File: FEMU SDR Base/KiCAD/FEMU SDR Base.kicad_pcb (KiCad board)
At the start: 4 copper layers, 164.8 x 164.8 mm, 94 parts, among them M1 M1, M10 M1, M11 M1, M12 M1, M13 M1, M14 M1, M15 M1, M16 M1, M2 M1, M3 M1, M4 M1, M5 M1, M6 M1, M7 M1, M8 M1, M9 M1, P1 Battery, P10 PWM2, P11 PWM3, P12 PWM4, P13 PWM1, P14 PWM2, P15 PWM3, P16 PWM4, P17 12V, P18 GND, P19 12V, P2 SDR_Shield_1, P20 GND, P21 SDR0, P22 SDR1, P27 PWM0, P28 PWM5, P29 PWM6, P3 SDR_Shield_2, P30 PWM7, P31 PWM0, P32 PWM5, P33 PWM6, P34 PWM7, P35 Battery, P36 RPi, P37 PXH, P38 Rx, P4 12V, P5 GND, P6 12V, P7 GND, P8 Raspi_Power_Shield, P9 PWM1, U1 TPS562209, U2 LP38858-LDO, U3 LP38858-LDO, U4 7833, U5 7833

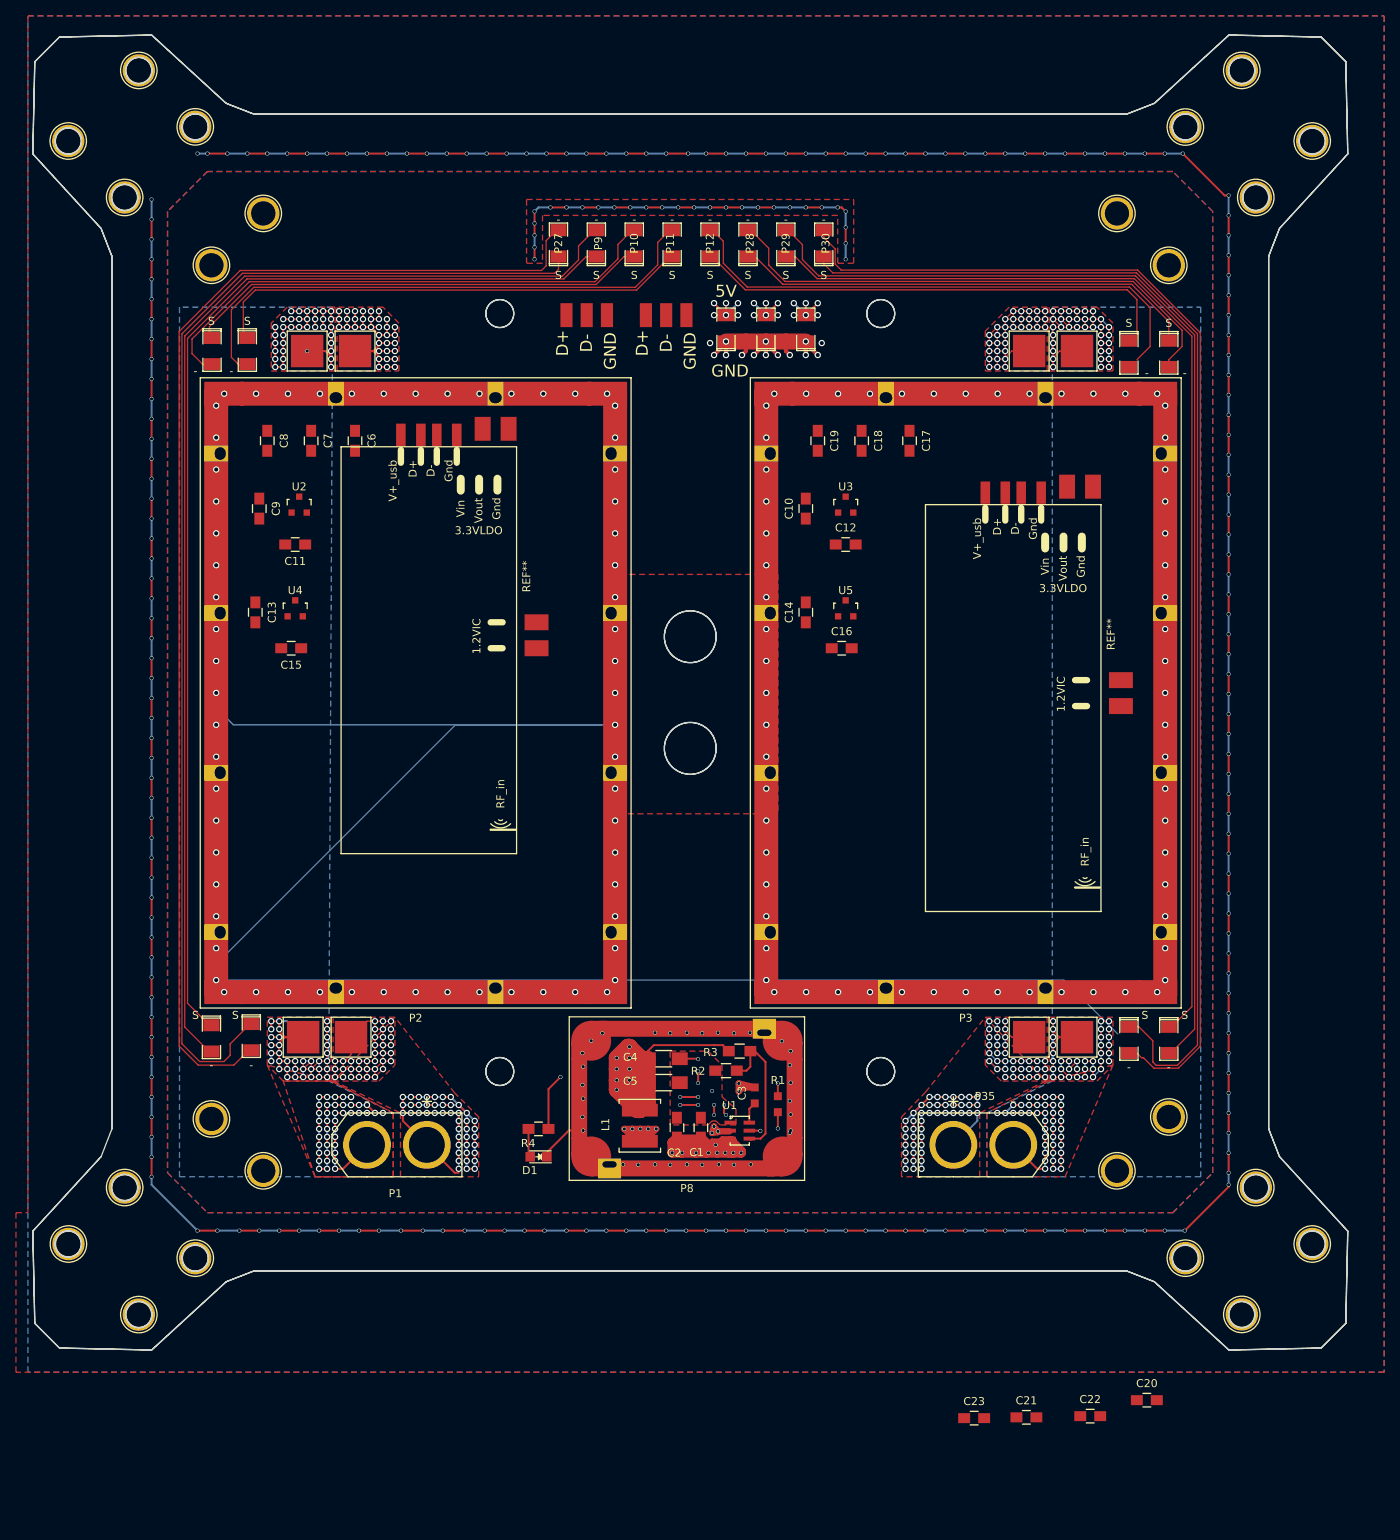
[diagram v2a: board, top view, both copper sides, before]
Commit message: STATUS=FREE, SDR1 arranged
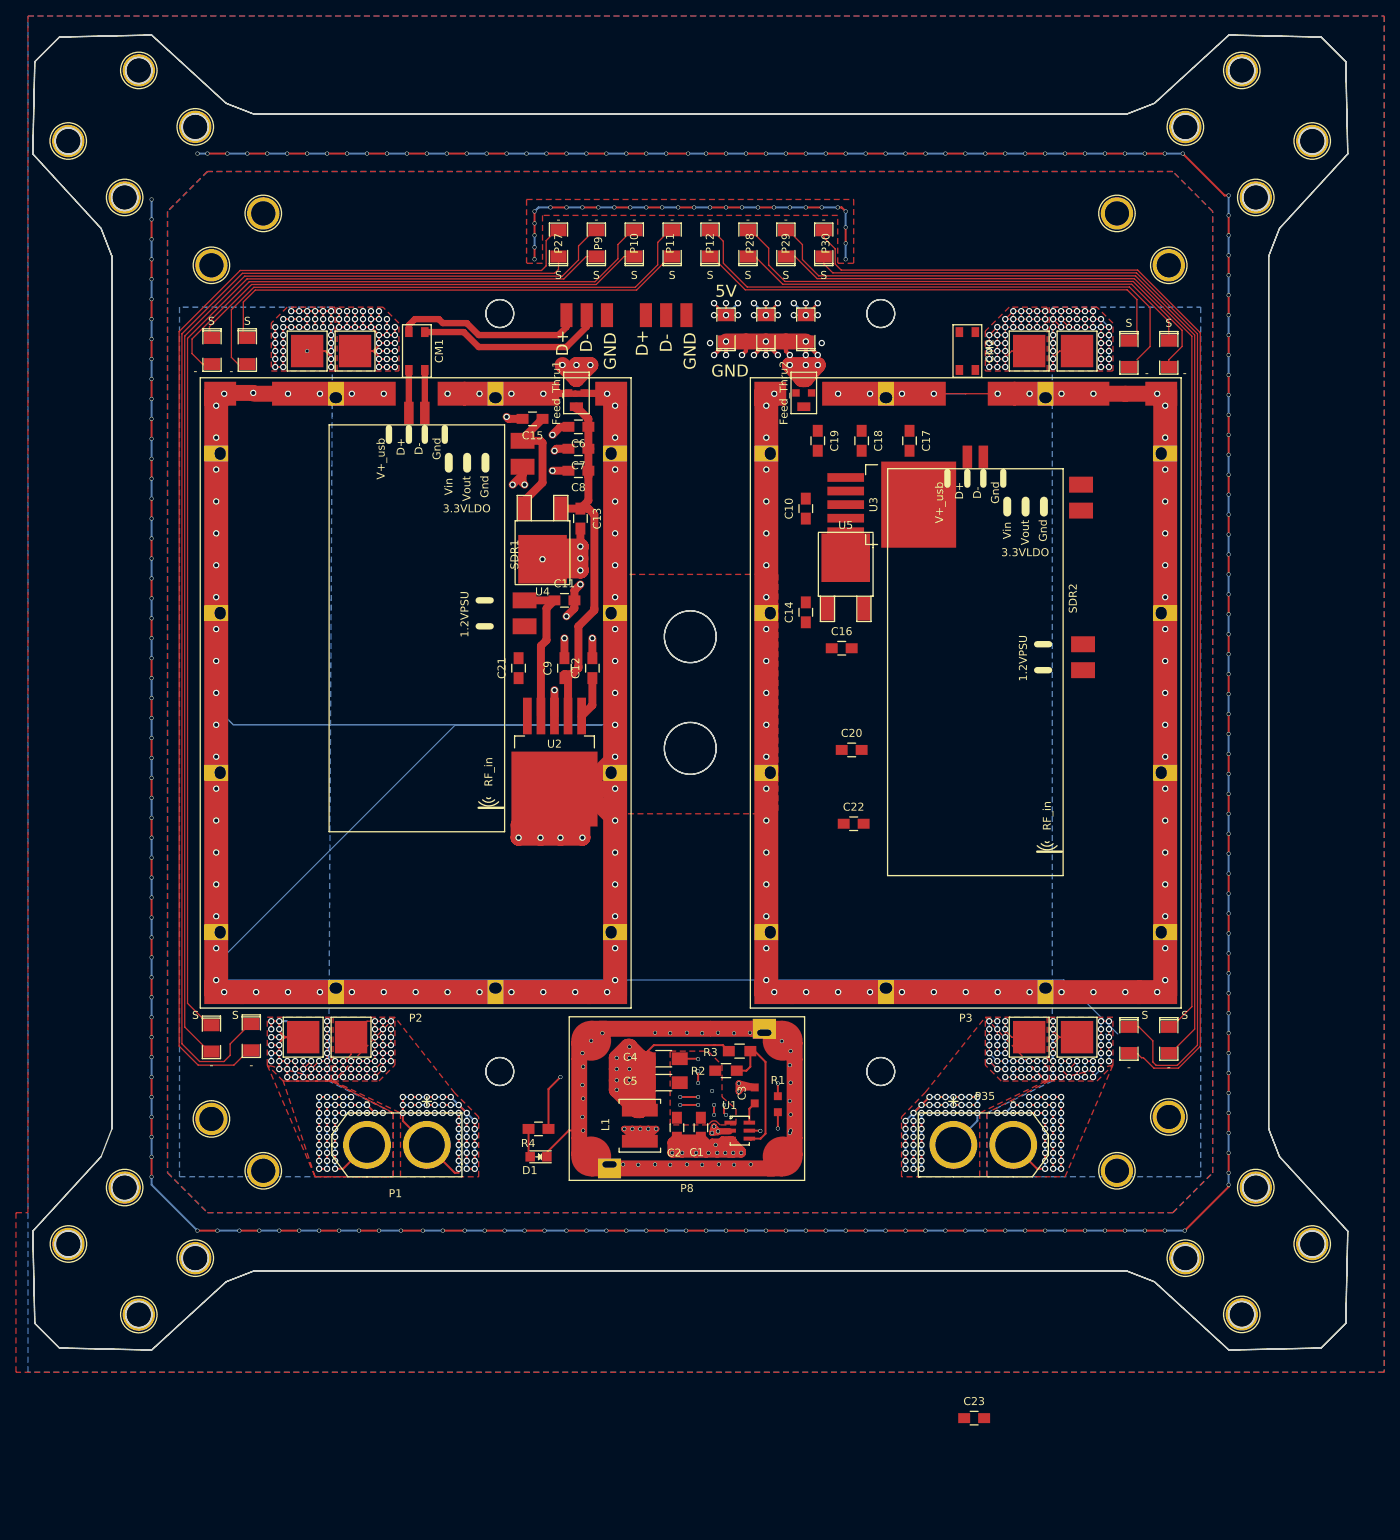
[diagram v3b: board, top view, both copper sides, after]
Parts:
- removed the REF** at (40.8, 104.8)
- removed the REF** at (114.0, 112.0)
- added CM1: CM_Fltr, ARB_foots:TDK_ACM_CM_filter, F.Cu at (50.2, 41.8)
- added CM2: CM_Fltr, ARB_foots:TDK_ACM_CM_filter, F.Cu at (119.2, 41.8)
- added Feed_Thru1: Feed_Thru, ARB_foots:AVX_W#F_FeedThrough_SMD_Caps, F.Cu at (70.2, 47.0)
- added Feed_Thru2: Feed_Thru, ARB_foots:AVX_W#F_FeedThrough_SMD_Caps, F.Cu at (98.8, 47.0)
- added SDR1: SDR_hack_foot, ARB_foots:SDR_hack_outline, F.Cu at (39.2, 102.0)
- added SDR2: SDR_hack_foot, ARB_foots:SDR_hack_outline, F.Cu at (109.2, 107.5)
- U2, U3: footprint TO_SOT_Packages_SMD:SOT-23 -> TO_SOT_Packages_SMD:TO-263-5Lead
- U4, U5: value 7833 -> LM1117; footprint TO_SOT_Packages_SMD:SOT-23 -> TO_SOT_Packages_SMD:TO-252-2Lead
- moved C21 113.4 mm to (63.0, 81.5), turned to 90 degrees
- moved C20 89.5 mm to (104.8, 91.8)
- moved C22 80.0 mm to (105.0, 101.0)
- moved C9 43.2 mm to (68.8, 81.5), turned to 90 degrees
- moved C13 42.4 mm to (70.8, 62.8)
- moved C15 41.7 mm to (64.8, 50.2)
- moved U2 41.5 mm to (67.5, 87.5), turned to 270 degrees
- moved C8 39.2 mm to (70.5, 56.8), turned to 180 degrees
- moved C12 35.3 mm to (72.2, 81.5), turned to 90 degrees
- moved C11 34.5 mm to (68.8, 73.0), turned to 0 degrees
- moved C7 33.5 mm to (70.5, 54.0), turned to 180 degrees
- moved U4 33.4 mm to (66.0, 61.5), turned to 180 degrees
- moved C6 28.1 mm to (70.5, 51.2), turned to 180 degrees
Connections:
- C10 pad 1: +5V -> /5V_S1
- C11 pad 1: +1V2_SDR1 -> /1V2_S0
- C13 pad 1: +5V -> /5V_S0
- C14 pad 2: +5V -> /5V_S1
- C15 pad 1: +3V3_SDR1 -> /3V3_S0
- C16 pad 2: +3V3_SDR2 -> /3V3_S1
- C17 pad 1: +5V -> /5V_S1
- C18 pad 1: +5V -> /5V_S1
- C19 pad 1: +5V -> /5V_S1
- C21 pad 1: +5V -> /5V_S0
- C22 pad 1: +5V -> /5V_S1
- C23 pad 1: +1V2_SDR2 -> /1V2_S1
- C6 pad 1: +5V -> /5V_S0
- C7 pad 1: +5V -> /5V_S0
- C8 pad 1: +5V -> /5V_S0
- C9 pad 1: +5V -> /5V_S0
- P21 pad 3: Net-(P21-Pad3) -> GND
- P22 pad 3: Net-(P22-Pad3) -> GND
- U2 pad 2: +5V -> /5V_S0
- U3 pad 2: +5V -> /5V_S1
- U4 pad 1: (no net) -> /5V_S0
- U4 pad 2: (no net) -> GND
- U4 pad 3: (no net) -> /3V3_S0
- U5 pad 1: (no net) -> /5V_S1
- U5 pad 2: (no net) -> GND
- U5 pad 3: (no net) -> /3V3_S1
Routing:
- net GND: track 1748.0 -> 1889.7 mm, vias 649 -> 661
- net +5V: track 240.7 -> 292.2 mm, vias 23 -> 29
- net /5V_S0: track 0.00 -> 47.5 mm
- net Net-(CM1-Pad2): track 0.00 -> 23.7 mm
- net Net-(CM1-Pad1): track 0.00 -> 23.6 mm
- net /1V2_S0: track 0.00 -> 19.0 mm
- net /3V3_S0: track 0.00 -> 14.8 mm
- net /D-_S0: track 0.00 -> 5.38 mm
- net /D+_S0: track 0.00 -> 5.38 mm
- net Net-(C12-Pad1): track 0.00 -> 5.31 mm
- net Net-(SDR1-PadGND): track 0.00 -> 5.12 mm, vias 0 -> 2

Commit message: Moved 5V power lines and moved drawings to silkscreen layer
Signed-off-by: hardiepienaar <hardiepienaar@gmail.com>
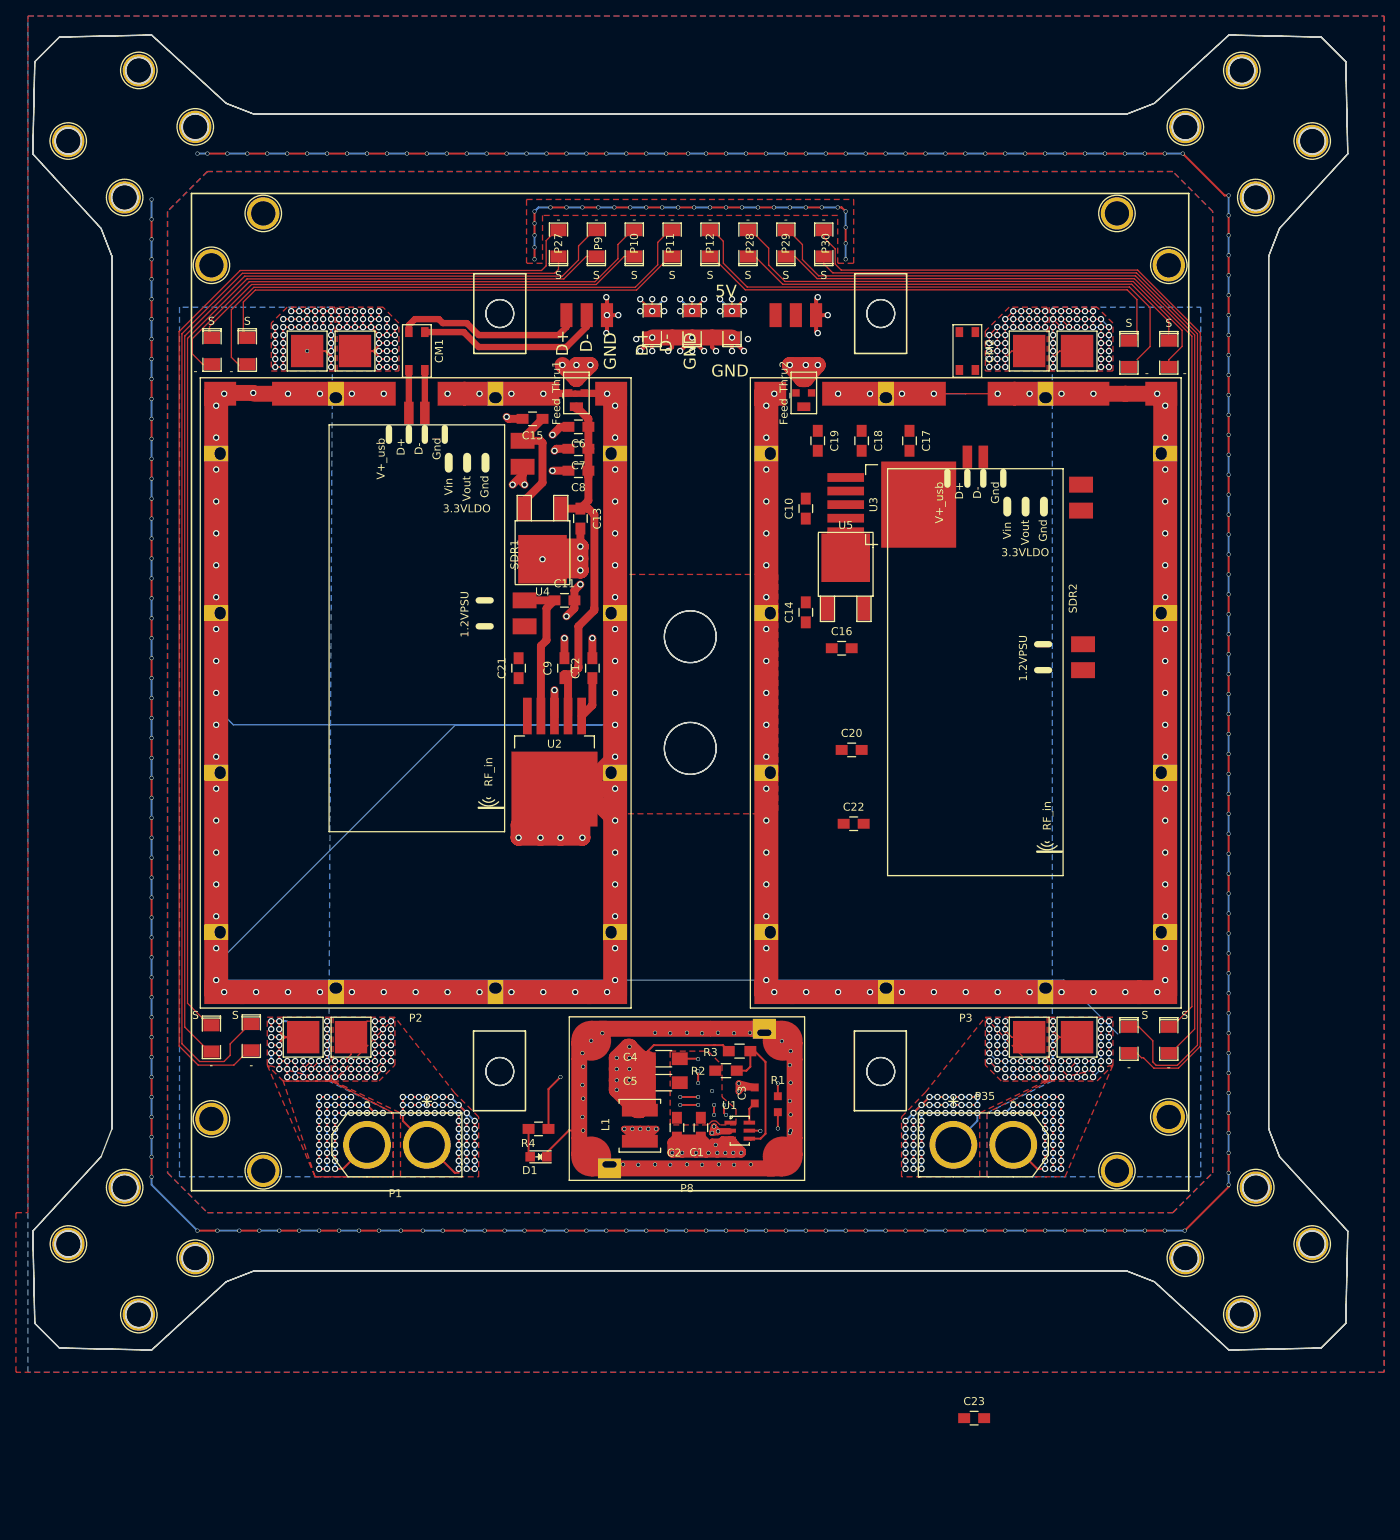
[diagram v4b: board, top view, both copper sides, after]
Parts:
- moved P22 16.2 mm to (97.8, 37.2)
- moved P36 9.26 mm to (89.8, 38.4)
- moved P37 9.26 mm to (84.8, 38.4)
- moved P38 9.26 mm to (79.8, 38.4)
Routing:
- net GND: track 1889.7 -> 1901.8 mm, vias 661 -> 668
- net +5V: track 292.2 -> 283.2 mm
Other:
- board text added: "Connect 5V line (Antheun) Add feedthroughs (Antheun) Add usb isolation (Antheun) Finish SDR layouts (Antheun) Add MESA logo Add FEMU logo Add Description Add Rev and date Add Sneaky signitures"
- board text removed: "Connect 5V line (Antheun) Add feedthroughs (Antheun) Add usb isolation (Antheun) Finish SDR layouts (Antheun) Add MESA logo Add FEMU logo Add Description Add Rev and date Add Sneaky signitures Add mechanical drawings to silkscreen"

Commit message: SDR2 populated
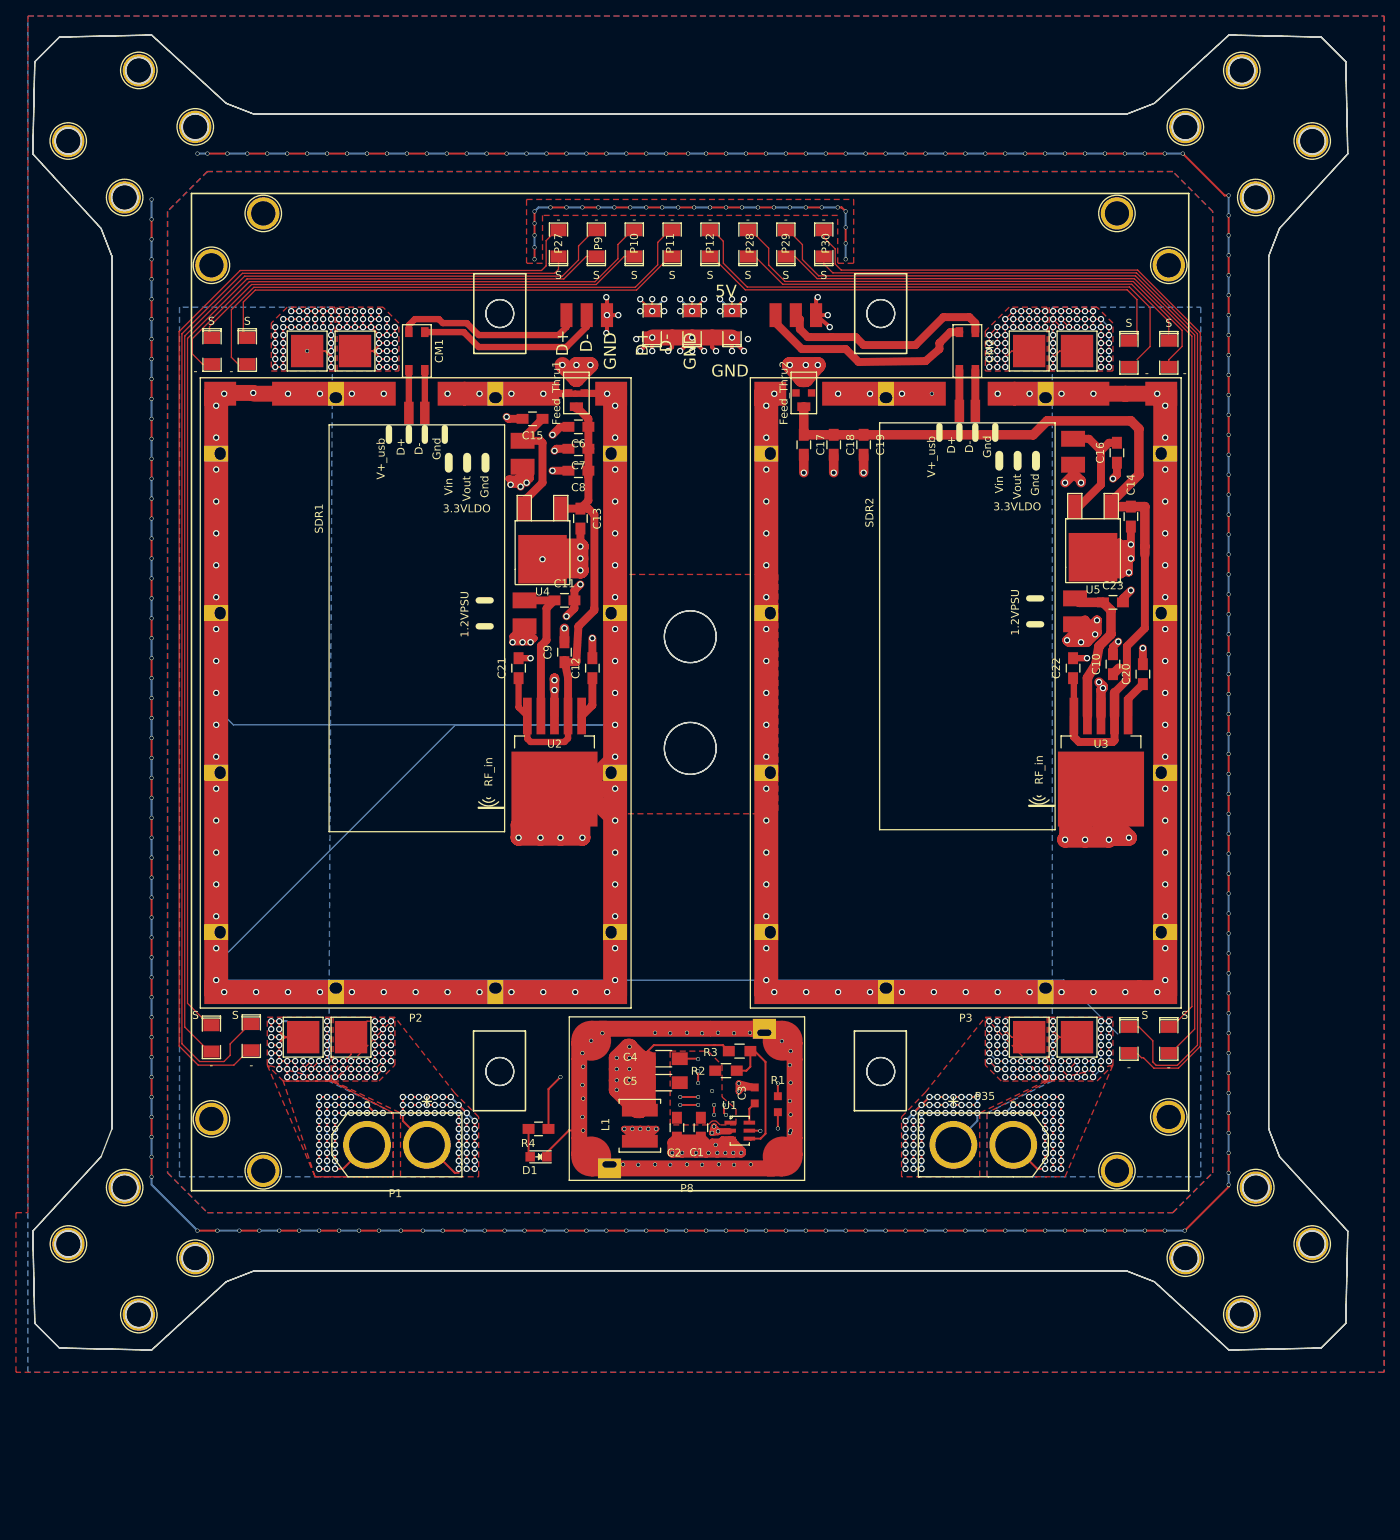
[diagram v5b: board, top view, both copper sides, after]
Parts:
- moved C23 103.7 mm to (137.5, 73.2)
- moved C10 43.2 mm to (137.5, 81.0)
- moved C14 42.5 mm to (139.8, 62.5)
- moved C16 42.3 mm to (138.0, 54.5), turned to 90 degrees
- moved U3 41.5 mm to (136.0, 87.5), turned to 270 degrees
- moved C20 37.7 mm to (141.2, 82.2), turned to 90 degrees
- moved C22 33.7 mm to (132.5, 81.5), turned to 90 degrees
- moved U5 33.5 mm to (135.0, 61.2), turned to 180 degrees
- moved C17 13.3 mm to (98.8, 53.5)
- moved SDR2 5.84 mm to (108.2, 101.8)
- moved C19 5.77 mm to (106.2, 53.5)
- moved C18 3.54 mm to (102.5, 53.5)
- moved C9 2.00 mm to (68.8, 79.5)
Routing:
- net /5V_S1: track 0.00 -> 107.8 mm
- net GND: track 1901.8 -> 2008.4 mm, vias 668 -> 687
- net Net-(SDR2-PadGND): track 0.00 -> 30.5 mm, vias 0 -> 6
- net Net-(CM2-Pad2): track 0.00 -> 27.9 mm
- net Net-(CM2-Pad1): track 0.00 -> 27.7 mm
- net Net-(SDR1-PadGND): track 5.12 -> 29.5 mm, vias 2 -> 6
- net /1V2_S1: track 0.00 -> 19.3 mm
- net /5V_S0: track 47.5 -> 64.3 mm
- net /3V3_S1: track 0.00 -> 15.2 mm
- net /D-_S1: track 0.00 -> 5.12 mm
- net /D+_S1: track 0.00 -> 5.12 mm
- net Net-(C20-Pad1): track 0.00 -> 4.77 mm
